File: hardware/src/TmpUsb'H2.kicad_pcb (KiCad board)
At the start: 2 copper layers, 26 x 17 mm, 20 parts, among them J1 B3B-PH-K, P1 215307, U1 PIC18F26J50

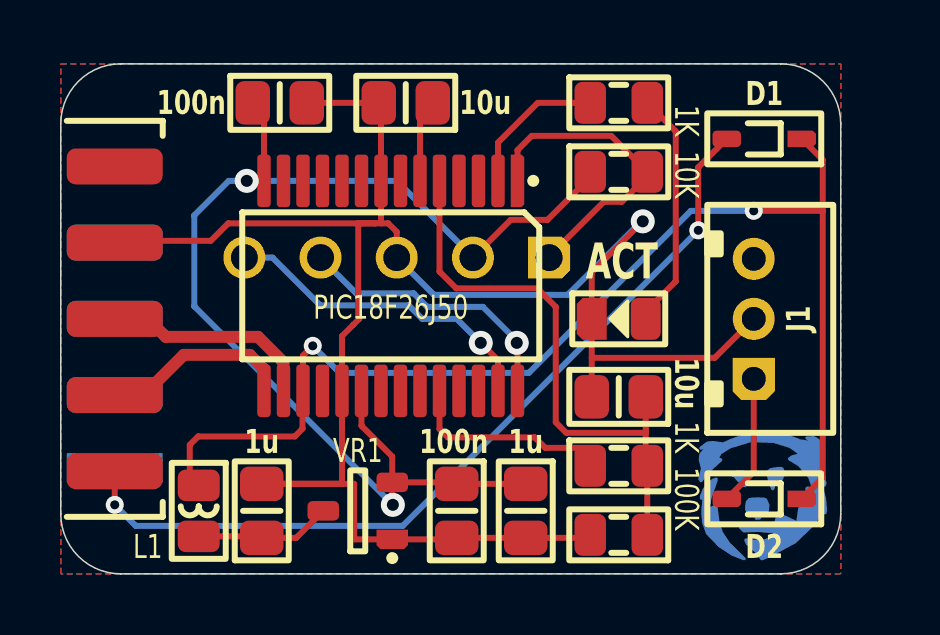
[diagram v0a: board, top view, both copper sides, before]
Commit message: Updating footprints
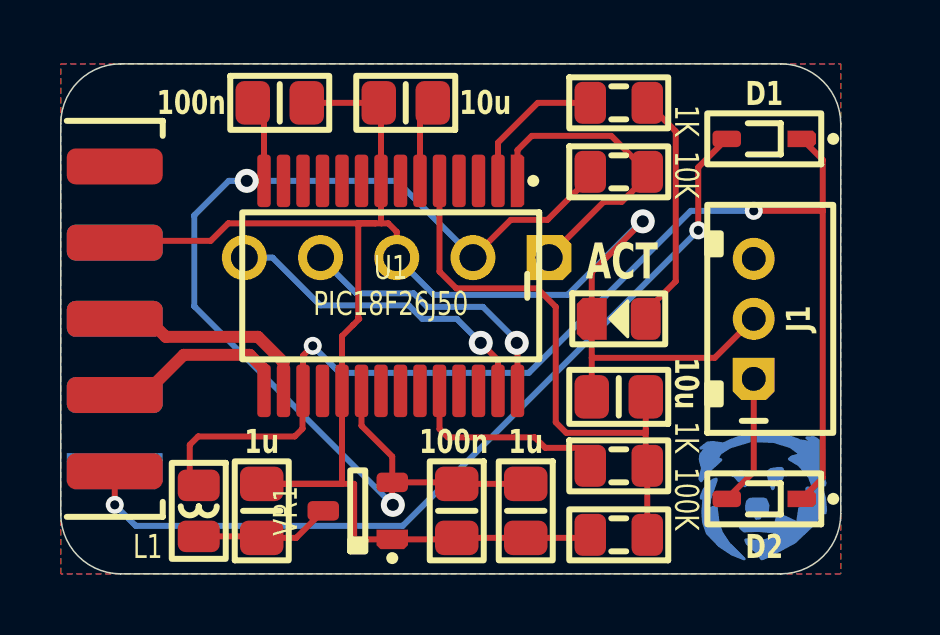
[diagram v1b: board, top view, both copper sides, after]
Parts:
- P1: footprint Medo64:P USB A 2.0 MB (9w) -> Medo64:J USB MB 2.0 Plug (9w)
- U1: footprint Medo64:U Micro PIC18F26J50 (SSOP-28) -> Medo64:U Micro [PIC18F26J50] (SSOP-28)
- VR1: footprint Medo64:VR Linear MCP1700 (SOT23-3) -> Medo64:VR Linear 3.3V 250mA [MCP1700] (SOT-23)

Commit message: Updated WOL connectort to AMP CT
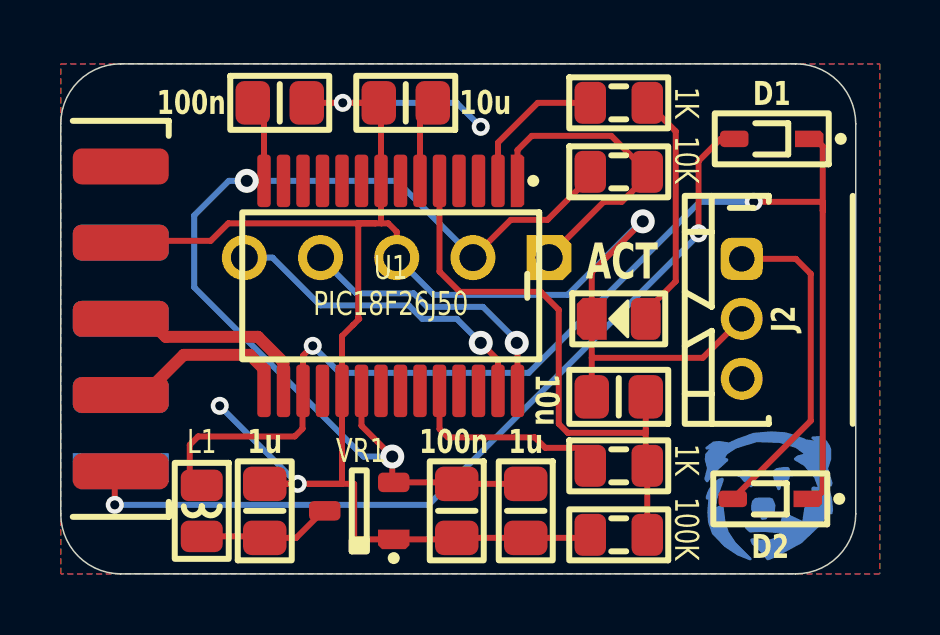
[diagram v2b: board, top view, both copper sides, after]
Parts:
- J1: renamed from P1; footprint Medo64:J USB MB 2.0 Plug (9w) -> Medo64:J USB MB 2.0 Edge (9w)
- J2: renamed from J1; value B3B-PH-K -> 292133-3; footprint Medo64:J JST PH B (3w) -> Medo64:J AMP 292133-3 [WOL] (3w)
- moved J2 0.40 mm to (37.7, 23.5), turned to -90 degrees
- moved D1 0.25 mm to (38.7, 17.5)
- moved Z? 0.20 mm to (38.6, 29.4)
- moved J1 0.20 mm to (17.0, 23.5)
- moved D2 0.20 mm to (38.6, 29.5)
- moved C3 0.10 mm to (21.8, 29.9)
- moved L1 0.10 mm to (19.7, 29.9)
- moved VR1 0.05 mm to (24.9, 29.9)
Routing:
- net GND: track 63.9 -> 74.4 mm, vias 1 -> 5
- net Vstby: track 4.37 -> 11.1 mm
- net +3.3V: track 39.4 -> 37.6 mm
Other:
- board size 26 x 17 mm -> 26.5 x 17 mm
- board text added: "TmpUsb'H2 BXXXX"
- board text removed: "TmpUsb'H2 B"

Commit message: Added case for H2 variant
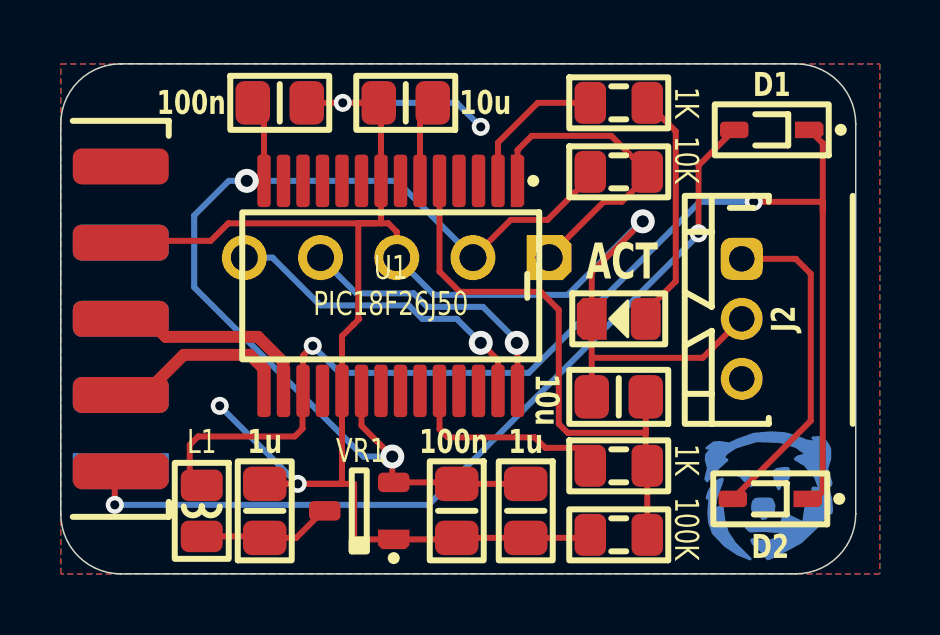
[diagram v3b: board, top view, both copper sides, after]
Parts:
- moved D1 0.30 mm to (38.7, 17.2)
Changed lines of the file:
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@@
 	(footprint "Medo64:D (SOD323)"
 		(layer "F.Cu")
-		(at 38.7 17.5 180)
+		(at 38.7 17.2 180)
 		(descr "CUS08F30,H3F")
 		(tags "SOD2612X116N")
@@
 	(segment
 		(start 40.4 19.9)
-		(end 40.4 17.75)
+		(end 40.4 17.65)
 		(width 0.2)
 		(layer "F.Cu")
@@
 	)
 	(segment
-		(start 40.4 17.75)
-		(end 40.15 17.5)
+		(start 40.4 17.65)
+		(end 39.95 17.2)
 		(width 0.2)
 		(layer "F.Cu")
@@
 	)
 	(segment
-		(start 37.65 17.5)
-		(end 37 17.5)
-		(width 0.2)
-		(layer "F.Cu")
-		(net 15)
-	)
-	(segment
-		(start 16.8 29.7)
-		(end 16.8 28.58)
+		(start 36.260361 18.389639)
+		(end 36.260361 20.65)
 		(width 0.2)
 		(layer "F.Cu")
@@
 	)
 	(segment
-		(start 36.260361 18.239639)
-		(end 36.260361 20.65)
+		(start 37.45 17.2)
+		(end 36.260361 18.389639)
 		(width 0.2)
 		(layer "F.Cu")
@@
 	)
 	(segment
-		(start 37 17.5)
-		(end 36.260361 18.239639)
+		(start 16.8 29.7)
+		(end 16.8 28.58)
 		(width 0.2)
 		(layer "F.Cu")
